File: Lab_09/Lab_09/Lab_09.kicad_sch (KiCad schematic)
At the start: 19 parts

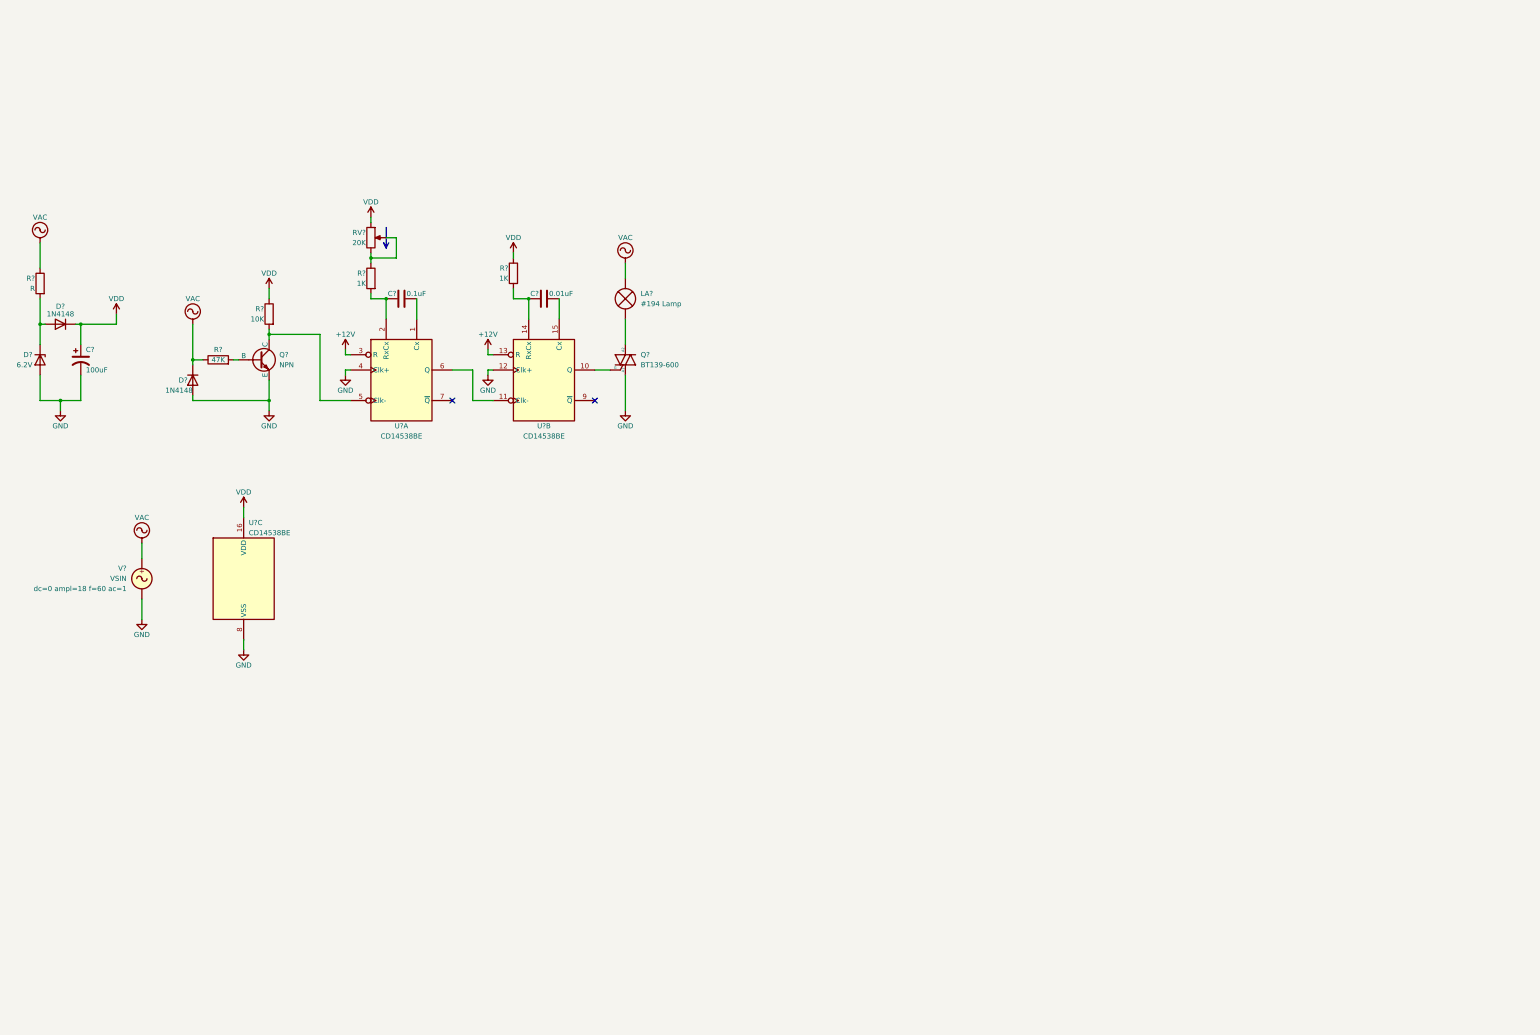
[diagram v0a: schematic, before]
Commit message: Finish Lab 9
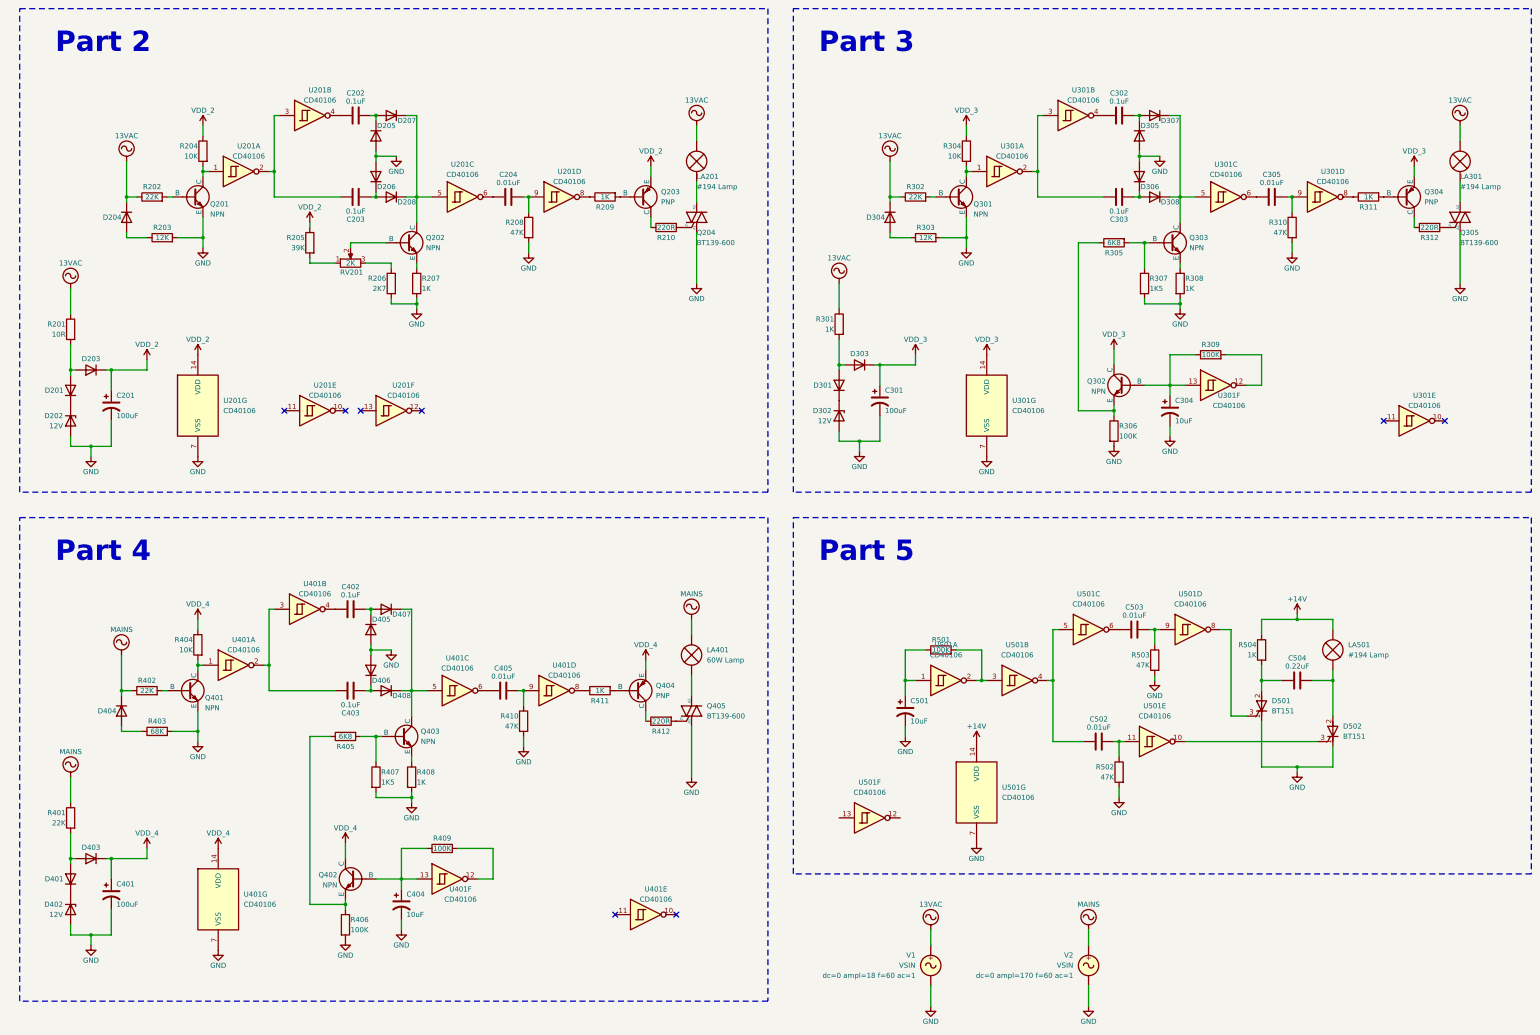
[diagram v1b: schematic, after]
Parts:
- removed C?: 0.1uF, symbol Device:C
- removed C?: 0.01uF, symbol Device:C
- removed R? (x2): 1K, symbol Device:R
- removed RV?: 20K, symbol Device:R_Potentiometer
- removed U? (x3): CD14538BE, Package_DIP:DIP-16_W7.62mm, symbol LarryLab:CD14538BE
- added C202, C203, C302, C303, C402, C403: 0.1uF, symbol Device:C
- added C204, C305, C405, C502, C503: 0.01uF, symbol Device:C
- added C301, C401: 100uF, symbol Device:C_Polarized_US
- added C304, C404, C501: 10uF, symbol Device:C_Polarized_US
- added C504: 0.22uF, symbol Device:C
- added D201, D205, D206, D207, D208, D301, D303, D305, D306, D307, D308, D401, D403, D405, D406, D407, D408: 1N4148, Diode_THT:D_DO-35_SOD27_P7.62mm_Horizontal, symbol Diode:1N4148
- added D302, D402: 12V, symbol Device:D_Zener
- added D304, D404: 1N4148, symbol Device:D
- added D501, D502: BT151, symbol Device:Q_SCR_KAG
- added LA301, LA501: #194 Lamp, symbol Device:Lamp
- added LA401: 60W Lamp, symbol Device:Lamp
- added Q202, Q301, Q302, Q303, Q401, Q402, Q403: NPN, symbol Simulation_SPICE:NPN
- added Q203, Q304, Q404: PNP, symbol Simulation_SPICE:PNP
- added Q305, Q405: BT139-600, Package_TO_SOT_THT:TO-220-3_Vertical, symbol Triac_Thyristor:BT139-600
- added R203, R303: 12K, symbol Device:R
- added R205: 39K, symbol Device:R
- added R206: 2K7, symbol Device:R
- added R207, R209, R301, R308, R311, R408, R411, R504: 1K, symbol Device:R
- added R208, R310, R410, R502, R503: 47K, symbol Device:R
- added R210, R312, R412: 220R, symbol Device:R
- added R302, R401, R402: 22K, symbol Device:R
- added R304, R404: 10K, symbol Device:R
- added R305, R405: 6K8, symbol Device:R
- added R306, R309, R406, R409, R501: 100K, symbol Device:R
- added R307, R407: 1K5, symbol Device:R
- added R403: 68K, symbol Device:R
- added RV201: 2K, symbol Device:R_Potentiometer
- added U201, U301, U401, U501: CD40106, symbol LarryLab:CD40106
- added V2: VSIN, symbol Simulation_SPICE:VSIN
- D202: renamed from D?; value 6.2V -> 12V
- R201: renamed from R?; value R -> 10R
- R202: renamed from R?; value 47K -> 22K
- gave numbers to parts that had none: 8
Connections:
- net GND: now also C301.2, C304.2, C401.2, C404.2, C501.2, D205.2 (A), D206.2 (A), D302.2 (A), D305.2 (A), D306.2 (A), D402.2 (A), D405.2 (A), D406.2 (A), D501.1 (K), D502.1 (K), Q301.3 (E), Q305.1 (A1), Q401.3 (E), Q405.1 (A1), R203.2, R206.2, R207.2, R208.2, R303.2, R306.2, R307.2, R308.2, R310.2, R403.2, R406.2, R407.2, R408.2, R410.2, R502.2, R503.2, U201.7 (VSS), U301.7 (VSS), U401.7 (VSS), U501.7 (VSS), V2.2; no longer D204.2 (A)
- net at Q201.1 (C), R204.2: now also U201.1
- net at Q204.3 (G): now also R210.2
- net at D203.2 (A), R201.2: now also D201.2 (A); no longer D202.1 (K)
- net VAC renamed 13VAC
- net 13VAC: now also D304.1 (K), LA301.1 (-), R301.1, R302.1
- net VDD renamed VDD_2
- net VDD_2: now also Q203.3 (E), R205.1, U201.14 (VDD)
- new net: D307.1 (K), D308.1 (K), Q303.1 (C), U301.5
- new net: C303.2, D306.1 (K), D308.2 (A)
- new net: Q402.3 (E), R405.1, R406.1
- new net: C405.2, R410.1, U401.9
- new net: R309.2, U301.12
- new net: C304.1, Q302.2 (B), R309.1, U301.13
- new net: R409.2, U401.12
- new net: C404.1, Q402.2 (B), R409.1, U401.13
- new net: C503.2, R503.1, U501.9
- new net: C202.1, U201.4
- new net: C202.2, D205.1 (K), D207.2 (A)
- new net: Q301.1 (C), R304.2, U301.1
- new net: Q301.2 (B), R302.2
- new net: D301.2 (A), D303.2 (A), R301.2
- new net: D204.2 (A), R203.1
- new net: Q403.3 (E), R408.1
- new net: Q203.1 (C), R210.1
- new net: Q203.2 (B), R209.2
- new net: D502.3 (G), U501.10
- new net: C502.2, R502.1, U501.11
- new net: R411.1, U401.8
- new net: D301.1 (K), D302.1 (K)
- new net: D407.1 (K), D408.1 (K), Q403.1 (C), U401.5
- new net: C405.1, U401.6
- new net: C504.1, D501.2 (A), R504.2
- new net: C504.2, D502.2 (A), LA501.2 (+)
- new net: D207.1 (K), D208.1 (K), Q202.1 (C), U201.5
- new net: C203.2, D206.1 (K), D208.2 (A)
- new net: C303.1, U301.2, U301.3
- new net: C302.1, U301.4
- new net: R206.1, RV201.3
- new net: R311.1, U301.8
- new net: C305.2, R310.1, U301.9
- new net: C403.2, D406.1 (K), D408.2 (A)
- new net: Q304.2 (B), R311.2
- new net: C501.1, R501.1, U501.1
- new net: R501.2, U501.2, U501.3
- new net: Q304.1 (C), R312.1
- new net: Q305.3 (G), R312.2
- new net: C502.1, U501.4, U501.5
- new net: C402.2, D405.1 (K), D407.2 (A)
- new net: D304.2 (A), R303.1
- new net: Q303.2 (B), R305.2, R307.1
- new net: Q303.3 (E), R308.1
- new net: LA401.2 (+), Q405.2 (A2)
- new net: Q405.3 (G), R412.2
- new net: C204.1, U201.6
- new net: D401.2 (A), D403.2 (A), R401.2
- new net: D401.1 (K), D402.1 (K)
- new net: R209.1, U201.8
- new net: C204.2, R208.1, U201.9
- new net: Q404.1 (C), R412.1
- new net: Q302.3 (E), R305.1, R306.1
- new net: Q401.2 (B), R402.2
- new net: C302.2, D305.1 (K), D307.2 (A)
- new net: D404.2 (A), R403.1
- new net: C503.1, U501.6
- new net: R205.2, RV201.1
- new net: Q202.2 (B), RV201.2
- new net: C305.1, U301.6
- new net: Q403.2 (B), R405.2, R407.1
- new net: Q401.1 (C), R404.2, U401.1
- new net: C203.1, U201.2, U201.3
- new net: Q202.3 (E), R207.1
- new net: Q404.2 (B), R411.2
- new net: C402.1, U401.4
- new net: D201.1 (K), D202.1 (K)
- new net: C403.1, U401.2, U401.3
- new net: LA301.2 (+), Q305.2 (A2)
- new net: D501.3 (G), U501.8
- new net +14V: LA501.1 (-), R504.1, U501.14 (VDD)
- new net MAINS: D404.1 (K), LA401.1 (-), R401.1, R402.1, V2.1
- new net VDD_3: C301.1, D303.1 (K), Q302.1 (C), Q304.3 (E), R304.1, U301.14 (VDD)
- new net VDD_4: C401.1, D403.1 (K), Q402.1 (C), Q404.3 (E), R404.1, U401.14 (VDD)
- no-connect marks 2 -> 8
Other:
- note added: "Part 2"
- note added: "Part 3"
- note added: "Part 4"
- note added: "Part 5"
- company: (none) -> ZAM Industries, LLC
- title: (none) -> Thyristor Phase Control Circuits
- moved on the sheet: C201, D202, D203, D204, LA201, Q201, Q204, R201, R202, R204, V1
